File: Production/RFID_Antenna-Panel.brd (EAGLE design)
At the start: 97.3 x 63.2 mm, 75 parts, among them J1 U.FL, J2 U.FL, J3 U.FL

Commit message: Caopy Murata Design w/ Transparency for x02
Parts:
- added C19, C20, C25, C26, C31, C32, C37, C38, C43, C44: 9.3 pF, special_parts:0402
- added C21, C22, C27, C28, C33, C34, C39, C40, C45, C46: 9.0 pF, special_parts:0402
- added C23, C24, C29, C30, C35, C36, C41, C42, C47, C48: 5.66 pF, special_parts:0402
- added J4, J5, J6, J7, J8: U.FL, SparkFun-Connectors:U.FL
- added L16, L21, L26, L31, L36: 0.26 uH, special_parts:0402
- added L17, L18, L22, L23, L27, L28, L32, L33, L37, L38: 0.26 uH, special_parts:0603
- added L19, L20, L24, L25, L29, L30, L34, L35, L39, L40: 0.24 uH, special_parts:0603
- added R4, R5, R6, R7, R8: 4.28k, special_parts:0402
- added U$31, U$41, U$51, U$61, U$71: ANTENNA, special_parts:ANT
- added U$32, U$33, U$42, U$43, U$52, U$53, U$62, U$63, U$72, U$73: (no value), SparkX:SPARKX-LARGE
- added U$34, U$35, U$44, U$45, U$54, U$55, U$64, U$65, U$74, U$75: (no value), buzzard_labels:UHF_RFID_RING0
- added U$36, U$37, U$46, U$47, U$56, U$57, U$66, U$67, U$76, U$77: (no value), buzzard_labels:ANTENNA1
- added U$38, U$39, U$48, U$49, U$58, U$59, U$68, U$69, U$78, U$79: (no value), SparkFun-Aesthetics:OSHW-LOGO-S
- added U$40, U$50, U$60, U$70, U$80: (no value), SparkX:QWIIC_BOARD_MOUNT_HOLES
- moved E$3 50.8 mm to (96.3, 89.0)
- moved E$4 50.8 mm to (96.3, 89.0)
- moved E$1 43.7 mm to (6.86, 89.0)
- moved E$2 43.7 mm to (6.86, 89.0)
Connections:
- new net A10: C26.2, L23.2, R5.2, U$41.P$2, U$41.P$4
- new net A11: C31.1, L27.2, R6.1, U$51.P$1, U$51.P$3
- new net A12: C32.2, L28.2, R6.2, U$51.P$2, U$51.P$4
- new net A13: C37.1, L32.2, R7.1, U$61.P$1, U$61.P$3
- new net A14: C38.2, L33.2, R7.2, U$61.P$2, U$61.P$4
- new net A15: C43.1, L37.2, R8.1, U$71.P$1, U$71.P$3
- new net A16: C44.2, L38.2, R8.2, U$71.P$2, U$71.P$4
- new net A7: C19.1, L17.2, R4.1, U$31.P$1, U$31.P$3
- new net A8: C20.2, L18.2, R4.2, U$31.P$2, U$31.P$4
- new net A9: C25.1, L22.2, R5.1, U$41.P$1, U$41.P$3
- new net C1C4: C19.2, C21.1
- new net C1C5: C25.2, C27.1
- new net C1C6: C31.2, C33.1
- new net C1C7: C37.2, C39.1
- new net C1C8: C43.2, C45.1
- new net C2C3: C20.1, C22.1
- new net C2C5: C26.1, C28.1
- new net C2C6: C32.1, C34.1
- new net C2C7: C38.1, C40.1
- new net C2C8: C44.1, C46.1
- new net C3C3: C21.2, C22.2
- new net C3C5: C27.2, C28.2
- new net C3C6: C33.2, C34.2
- new net C3C7: C39.2, C40.2
- new net C3C8: C45.2, C46.2
- new net GND10: C35.1, J6.1, J6.2, L29.2
- new net GND12: C41.1, J7.1, J7.2, L34.2
- new net GND14: C47.1, J8.1, J8.2, L39.2
- new net GND6: C23.1, J4.1, J4.2, L19.2
- new net GND8: C29.1, J5.1, J5.2, L24.2
- new net L5C3: C24.2, J4.FEED, L20.1
- new net L5C4: C30.2, J5.FEED, L25.1
- new net L5C5: C36.2, J6.FEED, L30.1
- new net L5C7: C42.2, J7.FEED, L35.1
- new net L5C8: C48.2, J8.FEED, L40.1
- new net N$106: C48.1, L36.2, L38.1, L39.1
- new net N$107: C47.2, L36.1, L37.1, L40.2
- new net N$46: C24.1, L16.2, L18.1, L19.1
- new net N$47: C23.2, L16.1, L17.1, L20.2
- new net N$61: C30.1, L21.2, L23.1, L24.1
- new net N$62: C29.2, L21.1, L22.1, L25.2
- new net N$76: C36.1, L26.2, L28.1, L29.1
- new net N$77: C35.2, L26.1, L27.1, L30.2
- new net N$91: C42.1, L31.2, L33.1, L34.1
- new net N$92: C41.2, L31.1, L32.1, L35.2
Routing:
- net N$46: track 0.00 -> 5.93 mm
- net N$106: track 0.00 -> 5.93 mm
- net N$76: track 0.00 -> 5.93 mm
- net N$91: track 0.00 -> 5.93 mm
- net N$61: track 0.00 -> 5.93 mm
- net A16: track 0.00 -> 5.61 mm
- net A8: track 0.00 -> 5.61 mm
- net A12: track 0.00 -> 5.61 mm
- net A10: track 0.00 -> 5.61 mm
- net A14: track 0.00 -> 5.61 mm
- net A13: track 0.00 -> 5.55 mm
- net A11: track 0.00 -> 5.55 mm
- net A9: track 0.00 -> 5.55 mm
- net A7: track 0.00 -> 5.55 mm
- net A15: track 0.00 -> 5.55 mm
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- added copper zone on layer 1, net GND10
- added copper zone on layer 16, net GND10
- added copper zone on layer 1, net GND11
- added copper zone on layer 16, net GND11
- added copper zone on layer 1, net GND12
- added copper zone on layer 16, net GND12
- added copper zone on layer 1, net GND13
- added copper zone on layer 16, net GND13
- added copper zone on layer 1, net GND14
- added copper zone on layer 16, net GND14
- added copper zone on layer 1, net GND15
- added copper zone on layer 16, net GND15
- added copper zone on layer 1, net GND6
- added copper zone on layer 16, net GND6
- added copper zone on layer 1, net GND7
- added copper zone on layer 16, net GND7
- added copper zone on layer 1, net GND8
- added copper zone on layer 16, net GND8
- added copper zone on layer 1, net GND9
- added copper zone on layer 16, net GND9
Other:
- board size 97.3 x 63.2 mm -> 123.2 x 106.9 mm

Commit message: Add production for x02
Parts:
- removed C37, C38, C43, C44: 9.3 pF, special_parts:0402
- removed C39, C40, C45, C46: 9.0 pF, special_parts:0402
- removed C41, C42, C47, C48: 5.66 pF, special_parts:0402
- removed J7, J8: U.FL, SparkFun-Connectors:U.FL
- removed L31, L36: 0.26 uH, special_parts:0402
- removed L32, L33, L37, L38: 0.26 uH, special_parts:0603
- removed L34, L35, L39, L40: 0.24 uH, special_parts:0603
- removed R7, R8: 4.28k, special_parts:0402
- removed U$61, U$71: ANTENNA, special_parts:ANT
- removed U$62, U$63, U$72, U$73: (no value), SparkX:SPARKX-LARGE
- removed U$64, U$65, U$74, U$75: (no value), buzzard_labels:UHF_RFID_RING0
- removed U$66, U$67, U$76, U$77: (no value), buzzard_labels:ANTENNA1
- removed U$68, U$69, U$78, U$79: (no value), SparkFun-Aesthetics:OSHW-LOGO-S
- removed U$70, U$80: (no value), SparkX:QWIIC_BOARD_MOUNT_HOLES
- C1, C10, C11, C12, C13, C14, C15, C16, C17, C18, C19, C2, C20, C21, C22, C23, C24, C25, C26, C27, C28, C29, C3, C30, C31, C32, C33, C34, C35, C36, C4, C5, C6, C7, C8, C9, L1, L11, L16, L21, L26, L6, R1, R2, R3, R4, R5, R6: device special_parts:0402 -> special_parts:0402_MURATA
- L10, L12, L13, L14, L15, L17, L18, L19, L2, L20, L22, L23, L24, L25, L27, L28, L29, L3, L30, L4, L5, L7, L8, L9: device special_parts:0603 -> special_parts:0603_MURATA
- moved U$40 93.1 mm to (12.7, 64.0)
- moved C24 86.3 mm to (14.4, 51.6)
- moved L19 86.3 mm to (14.1, 52.9)
- moved J4 86.2 mm to (12.5, 48.0)
- moved C22 86.1 mm to (13.3, 55.6)
- moved L18 86.0 mm to (14.6, 54.7)
- moved L20 86.0 mm to (11.9, 51.6)
- moved C20 85.9 mm to (13.7, 56.7)
- moved L16 85.8 mm to (13.0, 54.0)
- moved C23 85.6 mm to (11.6, 52.9)
- moved C21 85.6 mm to (12.5, 55.6)
- moved C19 85.0 mm to (12.1, 56.7)
- moved L17 85.0 mm to (11.4, 54.7)
- moved U$32 84.6 mm to (12.7, 67.2)
- moved U$33 84.6 mm to (12.7, 67.2)
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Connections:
- removed net A13: C37.1, L32.2, R7.1, U$61.P$1, U$61.P$3
- removed net A14: C38.2, L33.2, R7.2, U$61.P$2, U$61.P$4
- removed net A15: C43.1, L37.2, R8.1, U$71.P$1, U$71.P$3
- removed net A16: C44.2, L38.2, R8.2, U$71.P$2, U$71.P$4
- removed net C1C7: C37.2, C39.1
- removed net C1C8: C43.2, C45.1
- removed net C2C7: C38.1, C40.1
- removed net C2C8: C44.1, C46.1
- removed net C3C7: C39.2, C40.2
- removed net C3C8: C45.2, C46.2
- removed net GND12: C41.1, J7.1, J7.2, L34.2
- removed net GND14: C47.1, J8.1, J8.2, L39.2
- removed net L5C7: C42.2, J7.FEED, L35.1
- removed net L5C8: C48.2, J8.FEED, L40.1
- removed net N$106: C48.1, L36.2, L38.1, L39.1
- removed net N$107: C47.2, L36.1, L37.1, L40.2
- removed net N$16: C12.1, L6.2, L8.1, L9.1
- removed net N$17: C11.2, L10.2, L6.1, L7.1
- removed net N$31: C18.1, L11.2, L13.1, L14.1
- removed net N$32: C17.2, L11.1, L12.1, L15.2
- removed net N$91: C42.1, L31.2, L33.1, L34.1
- removed net N$92: C41.2, L31.1, L32.1, L35.2
- new net N$1: C12.P$1, L6.P$2, L8.P$1, L9.P$1
- new net N$18: C18.P$1, L11.P$2, L13.P$1, L14.P$1
- new net N$19: C17.P$2, L11.P$1, L12.P$1, L15.P$2
- new net N$2: C11.P$2, L10.P$2, L6.P$1, L7.P$1
- net A1: now also C1.P$1, L2.P$2, R1.P$1; no longer C1.1, L2.2, R1.1
- net A10: now also C26.P$2, L23.P$2, R5.P$2; no longer C26.2, L23.2, R5.2
- net A11: now also C31.P$1, L27.P$2, R6.P$1; no longer C31.1, L27.2, R6.1
- net A12: now also C32.P$2, L28.P$2, R6.P$2; no longer C32.2, L28.2, R6.2
- net A2: now also C2.P$2, L3.P$2, R1.P$2; no longer C2.2, L3.2, R1.2
- net A3: now also C7.P$1, L7.P$2, R2.P$1; no longer C7.1, L7.2, R2.1
- net A4: now also C8.P$2, L8.P$2, R2.P$2; no longer C8.2, L8.2, R2.2
- net A5: now also C13.P$1, L12.P$2, R3.P$1; no longer C13.1, L12.2, R3.1
- net A6: now also C14.P$2, L13.P$2, R3.P$2; no longer C14.2, L13.2, R3.2
- net A7: now also C19.P$1, L17.P$2, R4.P$1; no longer C19.1, L17.2, R4.1
- net A8: now also C20.P$2, L18.P$2, R4.P$2; no longer C20.2, L18.2, R4.2
- net A9: now also C25.P$1, L22.P$2, R5.P$1; no longer C25.1, L22.2, R5.1
- net C1C1: now also C7.P$2, C9.P$1; no longer C7.2, C9.1
- net C1C2: now also C13.P$2, C15.P$1; no longer C13.2, C15.1
- net C1C3: now also C1.P$2, C3.P$1; no longer C1.2, C3.1
- net C1C4: now also C19.P$2, C21.P$1; no longer C19.2, C21.1
- net C1C5: now also C25.P$2, C27.P$1; no longer C25.2, C27.1
- net C1C6: now also C31.P$2, C33.P$1; no longer C31.2, C33.1
- net C2C1: now also C10.P$1, C8.P$1; no longer C10.1, C8.1
- net C2C2: now also C14.P$1, C16.P$1; no longer C14.1, C16.1
- net C2C3: now also C20.P$1, C22.P$1; no longer C20.1, C22.1
- net C2C4: now also C2.P$1, C4.P$1; no longer C2.1, C4.1
- net C2C5: now also C26.P$1, C28.P$1; no longer C26.1, C28.1
- net C2C6: now also C32.P$1, C34.P$1; no longer C32.1, C34.1
- net C3C1: now also C10.P$2, C9.P$2; no longer C10.2, C9.2
- net C3C2: now also C15.P$2, C16.P$2; no longer C15.2, C16.2
- net C3C3: now also C21.P$2, C22.P$2; no longer C21.2, C22.2
- net C3C4: now also C3.P$2, C4.P$2; no longer C3.2, C4.2
- net C3C5: now also C27.P$2, C28.P$2; no longer C27.2, C28.2
- net C3C6: now also C33.P$2, C34.P$2; no longer C33.2, C34.2
- net GND: now also C5.P$1, L4.P$2; no longer C5.1, L4.2
- net GND10: now also C35.P$1, L29.P$2; no longer C35.1, L29.2
- net GND2: now also C11.P$1, L9.P$2; no longer C11.1, L9.2
- net GND4: now also C17.P$1, L14.P$2; no longer C17.1, L14.2
- net GND6: now also C23.P$1, L19.P$2; no longer C23.1, L19.2
- net GND8: now also C29.P$1, L24.P$2; no longer C29.1, L24.2
- net L5C1: now also C12.P$2, L10.P$1; no longer C12.2, L10.1
- net L5C2: now also C18.P$2, L15.P$1; no longer C18.2, L15.1
- net L5C3: now also C24.P$2, L20.P$1; no longer C24.2, L20.1
- net L5C4: now also C30.P$2, L25.P$1; no longer C30.2, L25.1
- net L5C5: now also C36.P$2, L30.P$1; no longer C36.2, L30.1
- net L5C6: now also C6.P$2, L5.P$1; no longer C6.2, L5.1
- net N$46: now also C24.P$1, L16.P$2, L18.P$1, L19.P$1; no longer C24.1, L16.2, L18.1, L19.1
- net N$47: now also C23.P$2, L16.P$1, L17.P$1, L20.P$2; no longer C23.2, L16.1, L17.1, L20.2
- net N$6: now also C6.P$1, L1.P$2, L3.P$1, L4.P$1; no longer C6.1, L1.2, L3.1, L4.1
- net N$61: now also C30.P$1, L21.P$2, L23.P$1, L24.P$1; no longer C30.1, L21.2, L23.1, L24.1
- net N$62: now also C29.P$2, L21.P$1, L22.P$1, L25.P$2; no longer C29.2, L21.1, L22.1, L25.2
- net N$7: now also C5.P$2, L1.P$1, L2.P$1, L5.P$2; no longer C5.2, L1.1, L2.1, L5.2
- net N$76: now also C36.P$1, L26.P$2, L28.P$1, L29.P$1; no longer C36.1, L26.2, L28.1, L29.1
- net N$77: now also C35.P$2, L26.P$1, L27.P$1, L30.P$2; no longer C35.2, L26.1, L27.1, L30.2
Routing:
- net N$106: track 5.93 -> 0.00 mm
- net N$16: track 5.93 -> 0.00 mm, vias 0 -> 1
- net N$91: track 5.93 -> 0.00 mm
- net N$31: track 5.93 -> 0.00 mm, vias 0 -> 1
- net A16: track 5.61 -> 0.00 mm
- net A14: track 5.61 -> 0.00 mm
- net A13: track 5.55 -> 0.00 mm
- net A15: track 5.55 -> 0.00 mm
- net N$107: track 5.50 -> 0.00 mm
- net N$17: track 5.50 -> 0.00 mm, vias 0 -> 1
- net N$32: track 5.50 -> 0.00 mm, vias 0 -> 1
- net N$92: track 5.50 -> 0.00 mm
- net A5: track 5.55 -> 1.44 mm
- net A11: track 5.55 -> 1.44 mm
- net A3: track 5.55 -> 1.44 mm
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- removed copper zone on layer 1, net GND12
- removed copper zone on layer 16, net GND12
- removed copper zone on layer 1, net GND13
- removed copper zone on layer 16, net GND13
- removed copper zone on layer 1, net GND14
- removed copper zone on layer 16, net GND14
- removed copper zone on layer 1, net GND15
- removed copper zone on layer 16, net GND15
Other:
- board size 123.2 x 106.9 mm -> 97.3 x 96.8 mm

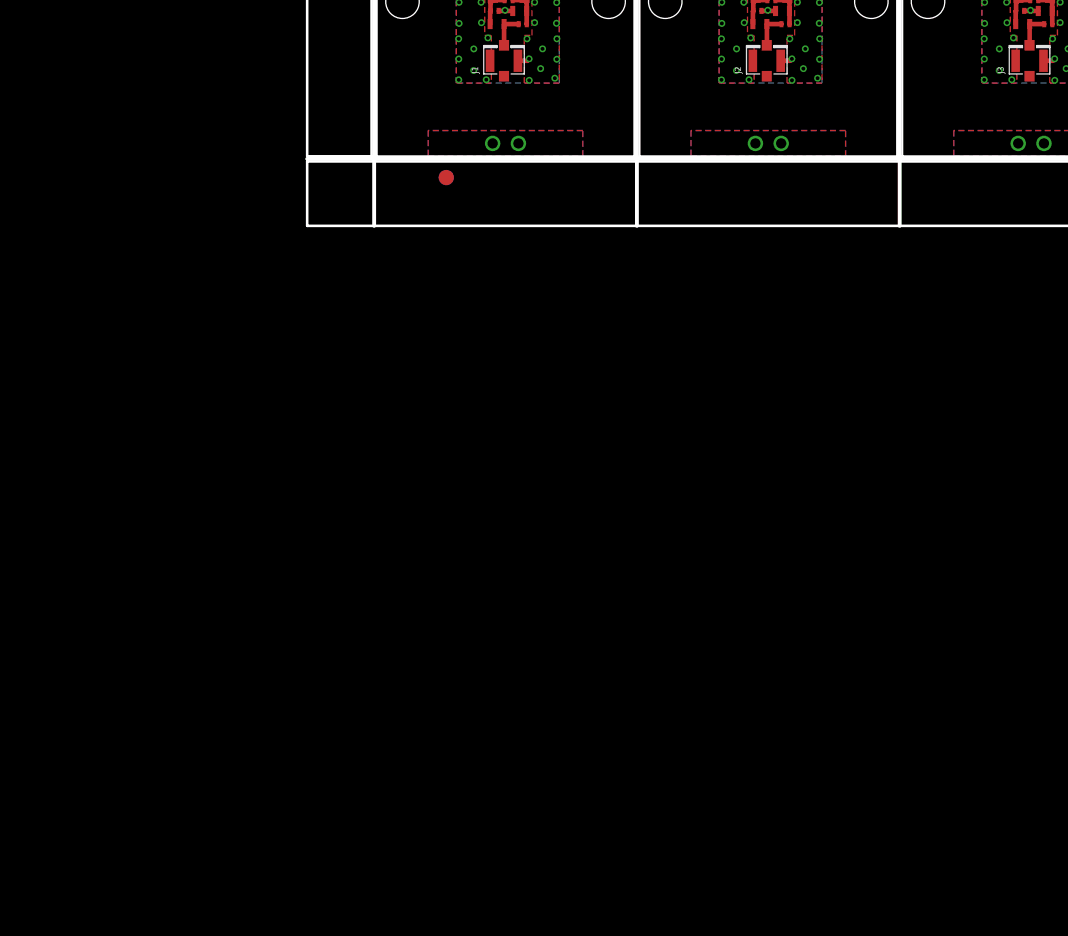
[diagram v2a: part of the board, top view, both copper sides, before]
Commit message: Updated production to match single file
* Updated component values were not reflected in production file
* Ran panelization script on correct board
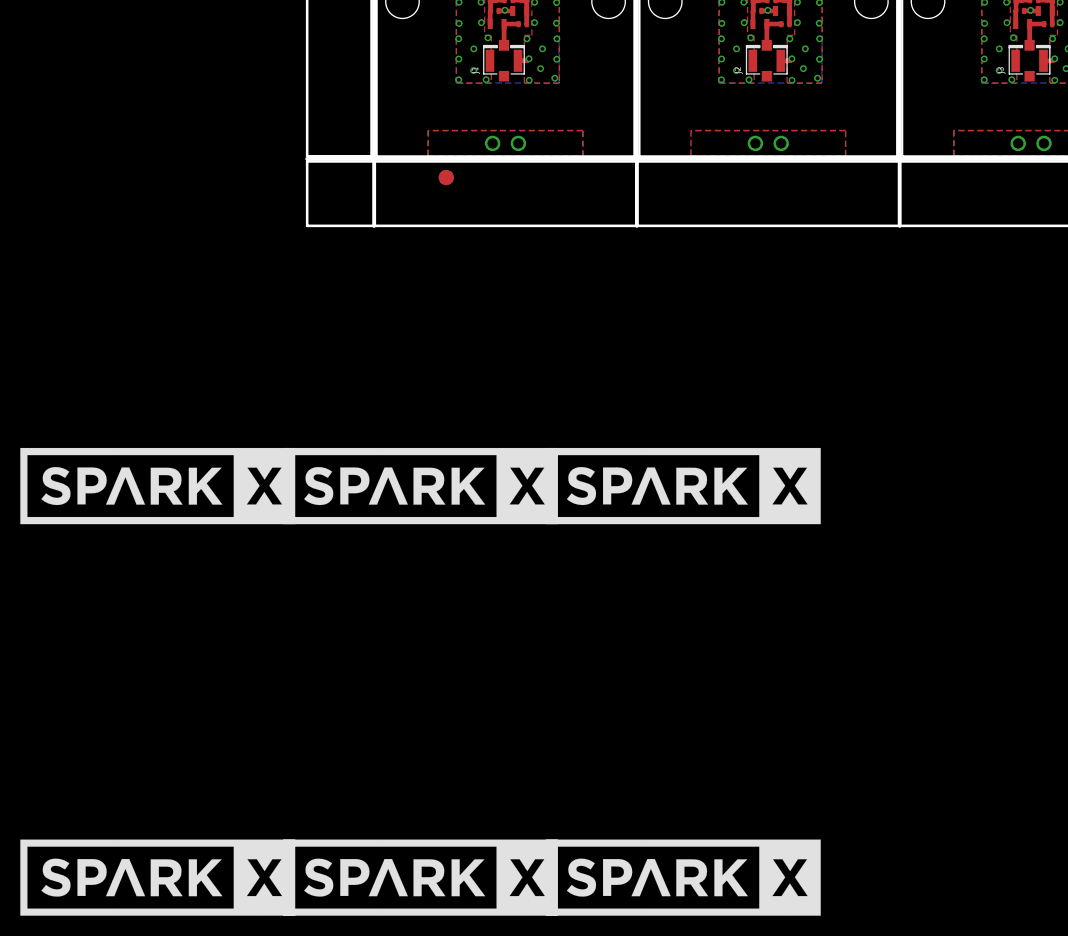
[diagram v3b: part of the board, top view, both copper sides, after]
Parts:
- added FRAME1, FRAME2, FRAME3, FRAME4, FRAME5, FRAME6: FRAME-LETTER, SparkFun-Aesthetics:CREATIVE_COMMONS
- added U$61, U$62: (no value), buzzard_labels:ANTENNA1
- added U$63, U$64: (no value), SparkFun-Aesthetics:OSHW-LOGO-S
- added U$65: (no value), SparkX:QWIIC_BOARD_MOUNT_HOLES
- added U$66: SPARKX-LOGO6, SparkX:SPARKX-XLARGE
- C1, C13, C14, C19, C2, C20, C25, C26, C31, C32, C7, C8: value 9.3 pF -> 5.0 pF
- C10, C15, C16, C21, C22, C27, C28, C3, C33, C34, C4, C9: value 9.0 pF -> 5.0 pF
- C11, C12, C17, C18, C23, C24, C29, C30, C35, C36, C5, C6: value 5.66 pF -> 2.4 pF
- L1, L11, L16, L21, L26, L6: value 0.26 uH -> 19 nH
- L10, L14, L15, L19, L20, L24, L25, L29, L30, L4, L5, L9: value 0.24 uH -> 11 nH
- L12, L13, L17, L18, L2, L22, L23, L27, L28, L3, L7, L8: value 0.26 uH -> 24 nH
- U$12, U$22, U$33: value (none) -> SPARKX-LOGO6; device SparkX:SPARKX-LARGE -> SparkX:SPARKX-XLARGE
- U$14, U$24, U$25, U$35: device buzzard_labels:UHF_RFID_RING0 -> SparkX:SPARKX-LARGE
- U$16, U$26, U$27, U$37: device buzzard_labels:ANTENNA1 -> buzzard_labels:UHF_RFID_RING0
- U$18, U$28, U$29, U$39: device SparkFun-Aesthetics:OSHW-LOGO-S -> buzzard_labels:ANTENNA1
- U$20, U$30: device SparkX:QWIIC_BOARD_MOUNT_HOLES -> SparkFun-Aesthetics:OSHW-LOGO-S
- U$21: value ANTENNA -> (none); device special_parts:ANT -> SparkX:QWIIC_BOARD_MOUNT_HOLES
- U$23: value (none) -> ANTENNA; device SparkX:SPARKX-LARGE -> special_parts:ANT
- U$31, U$41: value ANTENNA -> (none); device special_parts:ANT -> SparkFun-Aesthetics:OSHW-LOGO-S
- U$32, U$43: device SparkX:SPARKX-LARGE -> SparkX:QWIIC_BOARD_MOUNT_HOLES
- U$34, U$45: value (none) -> ANTENNA; device buzzard_labels:UHF_RFID_RING0 -> special_parts:ANT
- U$36, U$46, U$47, U$57: device buzzard_labels:ANTENNA1 -> SparkX:SPARKX-LARGE
- U$38, U$48, U$49, U$59: device SparkFun-Aesthetics:OSHW-LOGO-S -> buzzard_labels:UHF_RFID_RING0
- U$40, U$50: device SparkX:QWIIC_BOARD_MOUNT_HOLES -> buzzard_labels:ANTENNA1
- U$42, U$52, U$53: device SparkX:SPARKX-LARGE -> SparkFun-Aesthetics:OSHW-LOGO-S
- U$44, U$55: value (none) -> SPARKX-LOGO6; device buzzard_labels:UHF_RFID_RING0 -> SparkX:SPARKX-XLARGE
- U$51: value ANTENNA -> (none); device special_parts:ANT -> buzzard_labels:ANTENNA1
- U$54: device buzzard_labels:UHF_RFID_RING0 -> SparkX:QWIIC_BOARD_MOUNT_HOLES
- U$56: value (none) -> ANTENNA; device buzzard_labels:ANTENNA1 -> special_parts:ANT
- U$58: device SparkFun-Aesthetics:OSHW-LOGO-S -> SparkX:SPARKX-LARGE
- U$60: device SparkX:QWIIC_BOARD_MOUNT_HOLES -> buzzard_labels:UHF_RFID_RING0
- moved U$33 139.4 mm to (30.2, -71.1), flipped to the top
- moved U$55 117.3 mm to (4.32, -32.5), flipped to the top
- moved U$12 116.5 mm to (-21.6, -71.1)
- moved U$22 116.5 mm to (4.32, -71.1)
- moved U$44 111.2 mm to (-21.6, -32.5)
- moved U$31 68.1 mm to (64.5, 21.1)
- moved U$32 66.6 mm to (64.5, 25.4), flipped to the bottom
- moved U$52 27.0 mm to (38.6, 59.7), flipped to the bottom
- moved U$53 27.0 mm to (38.6, 59.7), flipped to the top
- moved U$42 27.0 mm to (12.7, 59.7)
- moved U$41 26.5 mm to (12.7, 59.7), flipped to the bottom
- moved U$43 26.1 mm to (12.7, 64.0)
- moved U$21 25.9 mm to (38.6, 25.4), flipped to the bottom
- moved U$51 22.1 mm to (42.6, 62.7), flipped to the bottom
- moved U$54 20.0 mm to (38.6, 64.0), flipped to the bottom
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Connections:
- net A10: now also U$45.P$2, U$45.P$4; no longer U$41.P$2, U$41.P$4
- net A11: now also U$56.P$1, U$56.P$3; no longer U$51.P$1, U$51.P$3
- net A12: now also U$56.P$2, U$56.P$4; no longer U$51.P$2, U$51.P$4
- net A5: now also U$23.P$1, U$23.P$3; no longer U$21.P$1, U$21.P$3
- net A6: now also U$23.P$2, U$23.P$4; no longer U$21.P$2, U$21.P$4
- net A7: now also U$34.P$1, U$34.P$3; no longer U$31.P$1, U$31.P$3
- net A8: now also U$34.P$2, U$34.P$4; no longer U$31.P$2, U$31.P$4
- net A9: now also U$45.P$1, U$45.P$3; no longer U$41.P$1, U$41.P$3
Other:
- board text added: "Owen Lyke"
